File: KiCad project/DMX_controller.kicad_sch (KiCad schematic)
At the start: 8 parts, among them J1 DMX_output, SW1 SW_Push_DPDT, U1 TTL_to_RS485_transceiver

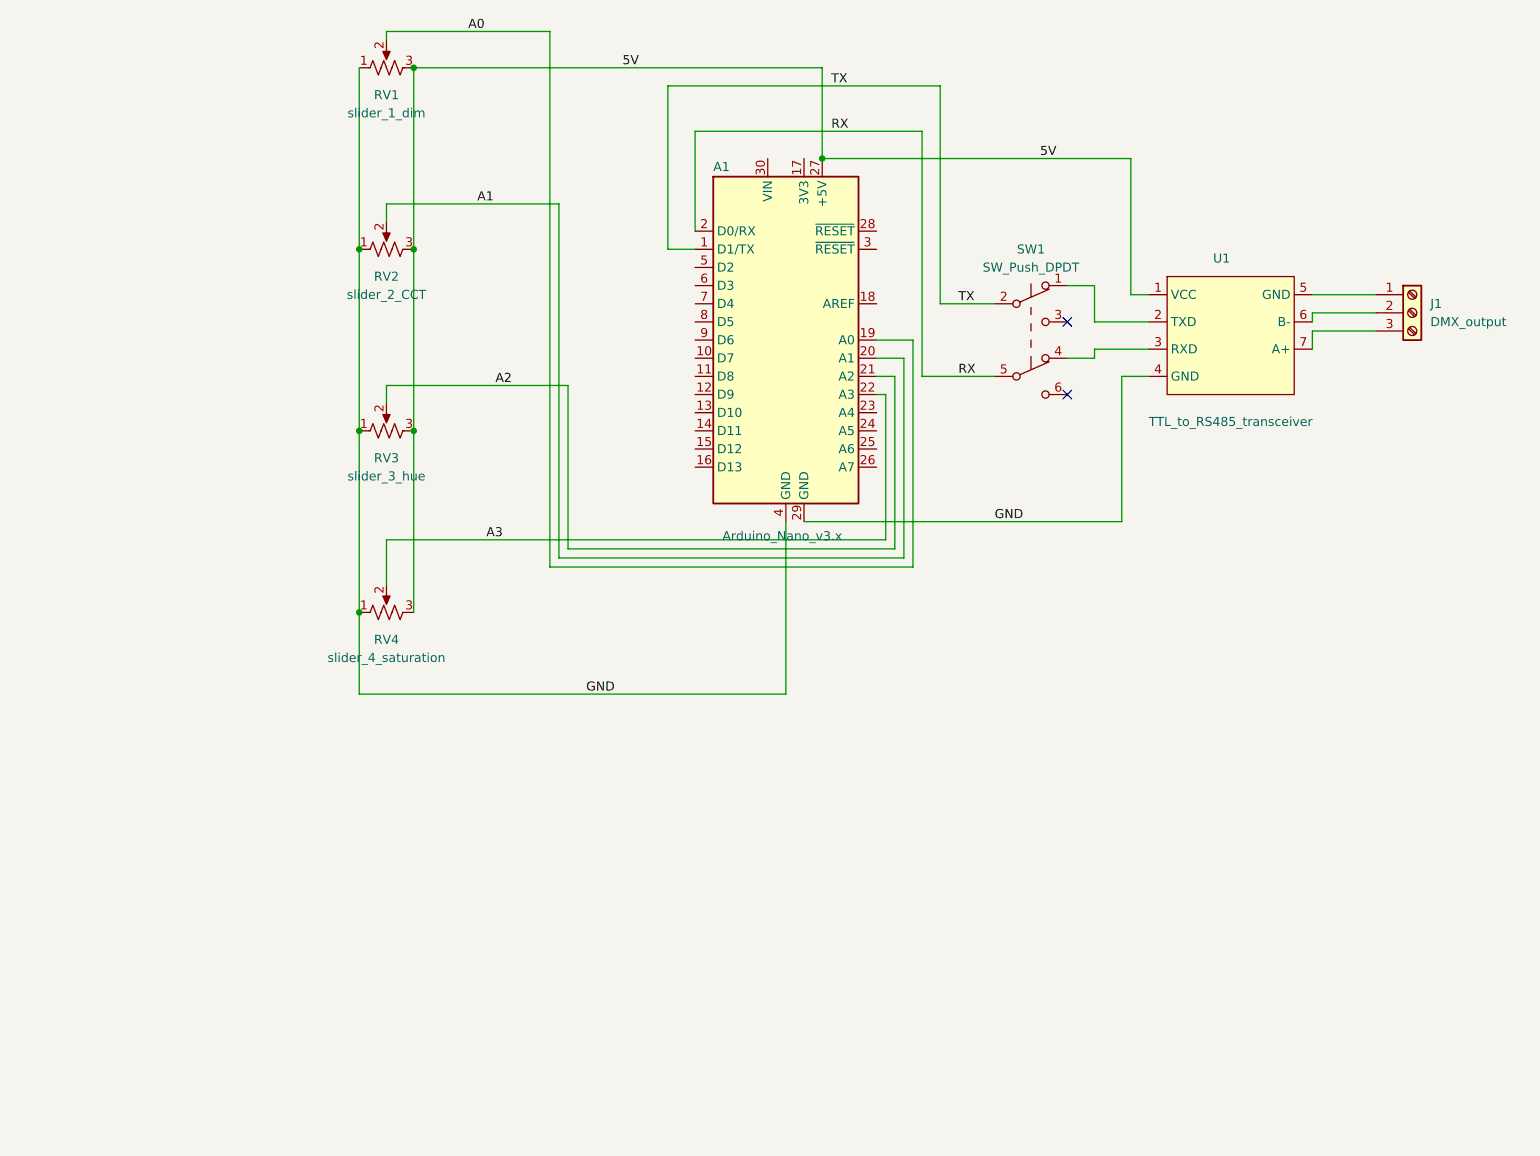
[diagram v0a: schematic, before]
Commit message: Clean up schematic
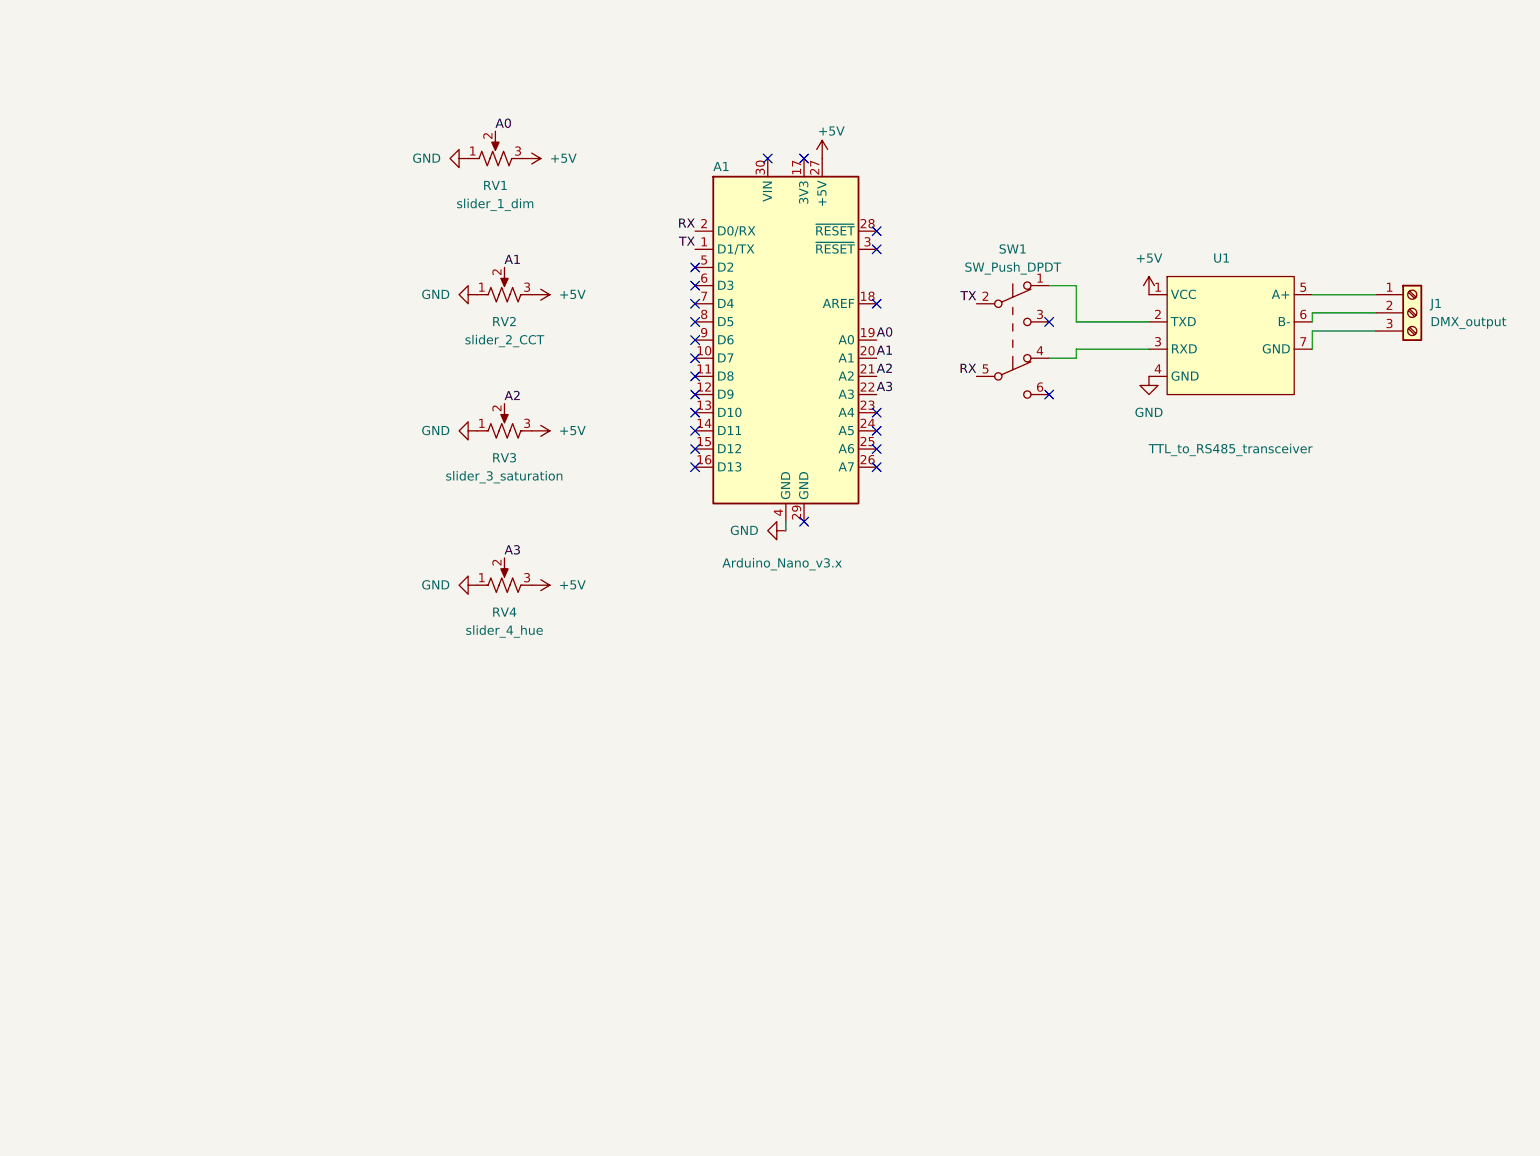
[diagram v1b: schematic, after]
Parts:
- RV3: value slider_3_hue -> slider_3_saturation
- RV4: value slider_4_saturation -> slider_4_hue
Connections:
- net GND: no longer A1.29 (GND)
- net 5V renamed +5V
- no-connect marks 2 -> 24
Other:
- title: (none) -> DMX controller
- moved on the sheet: RV1, RV2, RV3, RV4, SW1

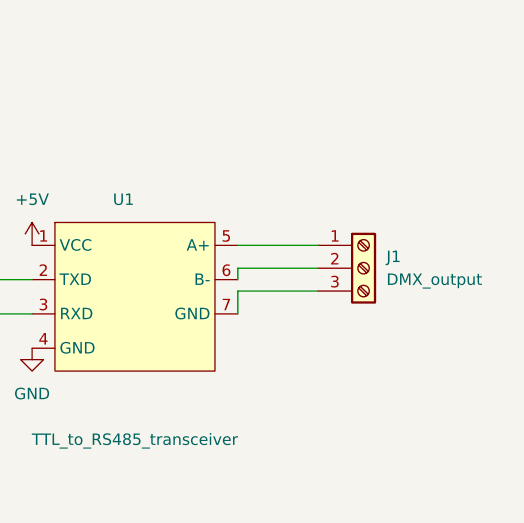
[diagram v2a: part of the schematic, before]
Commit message: Rotate screw terminal so 3D model is oriented
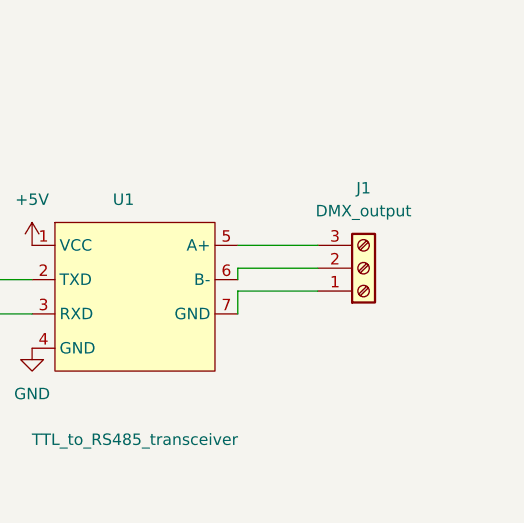
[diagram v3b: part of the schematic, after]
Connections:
- net at J1.1 (Pin_1): now also U1.7 (GND); no longer U1.5 (A+)
- net at J1.3 (Pin_3): now also U1.5 (A+); no longer U1.7 (GND)
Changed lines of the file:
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@@
     (pin "1")
   )
-  (symbol (lib_id "Connector:Screw_Terminal_01x03") (at 210.82 85.09 0) (unit 1)
+  (symbol (lib_id "Connector:Screw_Terminal_01x03") (at 210.82 85.09 0) (mirror x) (unit 1)
     (in_bom yes) (on_board yes) (fields_autoplaced)
-    (property "Reference" "J1" (id 0) (at 213.36 83.8199 0)
-      (effects (font (size 1.27 1.27)) (justify left))
-    )
-    (property "Value" "DMX_output" (id 1) (at 213.36 86.3599 0)
-      (effects (font (size 1.27 1.27)) (justify left))
-    )
+    (property "Reference" "J1" (id 0) (at 210.82 76.2 0))
+    (property "Value" "DMX_output" (id 1) (at 210.82 78.74 0))
     (property "Footprint" "TerminalBlock:TerminalBlock_bornier-3_P5.08mm" (id 2) (at 210.82 85.09 0)
       (effects (font (size 1.27 1.27)) hide)

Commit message: Add 3D models to slide pot and screw terminal
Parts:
- J1: footprint TerminalBlock:TerminalBlock_bornier-3_P5.08mm -> TerminalBlock_Phoenix:TerminalBlock_Phoenix_MKDS-3-3-5.08_1x03_P5.08mm_Horizontal
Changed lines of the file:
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@@
     (property "Reference" "J1" (id 0) (at 210.82 76.2 0))
     (property "Value" "DMX_output" (id 1) (at 210.82 78.74 0))
-    (property "Footprint" "TerminalBlock:TerminalBlock_bornier-3_P5.08mm" (id 2) (at 210.82 85.09 0)
+    (property "Footprint" "TerminalBlock_Phoenix:TerminalBlock_Phoenix_MKDS-3-3-5.08_1x03_P5.08mm_Horizontal" (id 2) (at 210.82 85.09 0)
       (effects (font (size 1.27 1.27)) hide)
     )
@@
     )
     (path "/0b856e1d-62f6-491f-9501-fb065244f252"
-      (reference "J1") (unit 1) (value "DMX_output") (footprint "TerminalBlock:TerminalBlock_bornier-3_P5.08mm")
+      (reference "J1") (unit 1) (value "DMX_output") (footprint "TerminalBlock_Phoenix:TerminalBlock_Phoenix_MKDS-3-3-5.08_1x03_P5.08mm_Horizontal")
     )
     (path "/de29216a-baed-4cb1-ab4e-d5a5a710d61b"

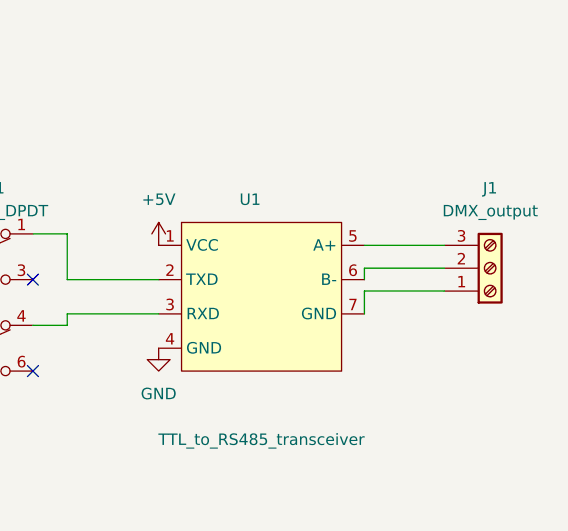
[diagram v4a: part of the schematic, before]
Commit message: Route DMX (RS-485) as differential pair
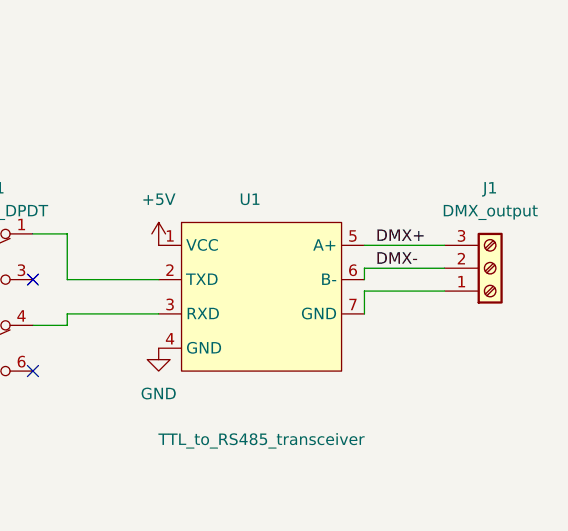
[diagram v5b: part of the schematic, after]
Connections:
- net DMX-: now reaches J1.2 (Pin_2), U1.6 (B-)
- net DMX+: now reaches J1.3 (Pin_3), U1.5 (A+)
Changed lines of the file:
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@@
+    (effects (font (size 1.27 1.27)) (justify left bottom))
+  )
+  (label "DMX-" (at 198.12 85.09 0)
     (effects (font (size 1.27 1.27)) (justify left bottom))
   )
@@
     (effects (font (size 1.27 1.27)) (justify left bottom))
   )
+  (label "DMX+" (at 198.12 82.55 0)
+    (effects (font (size 1.27 1.27)) (justify left bottom))
+  )

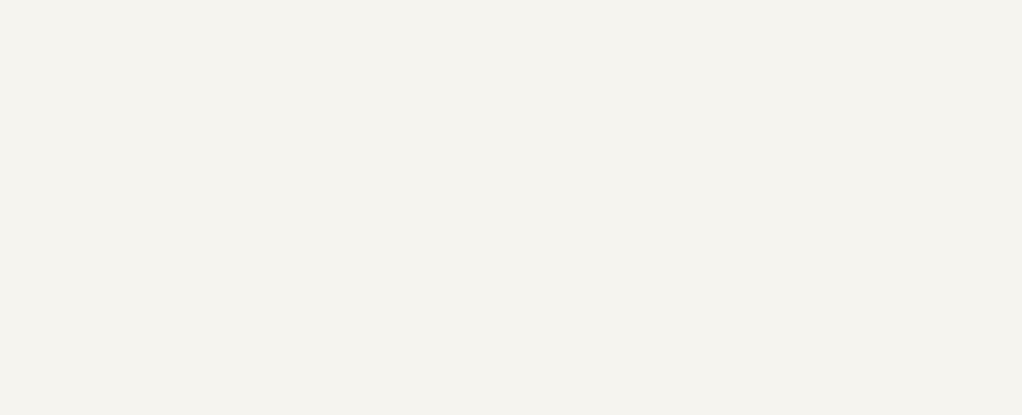
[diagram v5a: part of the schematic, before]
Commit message: Add CERN Open Hardware License Strongly Reciprocal
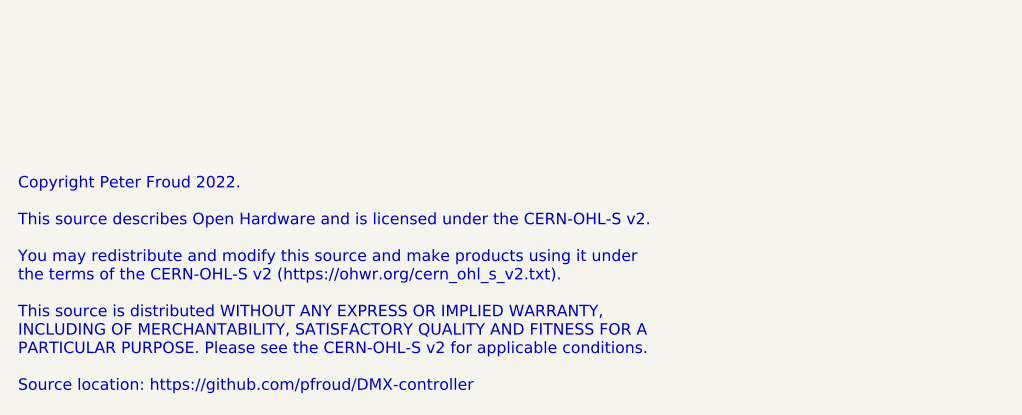
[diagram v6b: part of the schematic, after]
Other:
- note added: "Copyright Peter Froud 2022. This source describes Open Hardware and is licensed under the CERN-OHL-S v2. You may redistribute and modify this source and make products using it under the terms of the CERN-OHL-S v2 (https://ohwr.org/cern_ohl_s_v2.txt). This source is distributed WITHOUT ANY EXPRESS OR IMPLIED WARRANTY, INCLUDING OF MERCHANTABILITY, SATISFACTORY QUALITY AND FITNESS FOR A PARTICULAR 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"
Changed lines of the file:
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@@
     (stroke (width 0) (type default) (color 0 0 0 0))
+  )
+  (text "Copyright Peter Froud 2022.\n\nThis source describes Open Hardware and is licensed under the CERN-OHL-S v2.\n\nYou may redistribute and modify this source and make products using it under\nthe terms of the CERN-OHL-S v2 (https://ohwr.org/cern_ohl_s_v2.txt).\n\nThis source is distributed WITHOUT ANY EXPRESS OR IMPLIED WARRANTY,\nINCLUDING OF MERCHANTABILITY, SATISFACTORY QUALITY AND FITNESS FOR A\nPARTICULAR PURPOSE. Please see the CERN-OHL-S v2 for applicable conditions. \n\nSource location: https://github.com/pfroud/DMX-controller"
+    (at 15.24 200.66 0)
+    (effects (font (size 1.27 1.27)) (justify left bottom))
   )
   (label "A0" (at 135.89 88.9 0)
